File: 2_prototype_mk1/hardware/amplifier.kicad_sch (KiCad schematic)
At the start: 8 parts, among them U5 MAX98357A

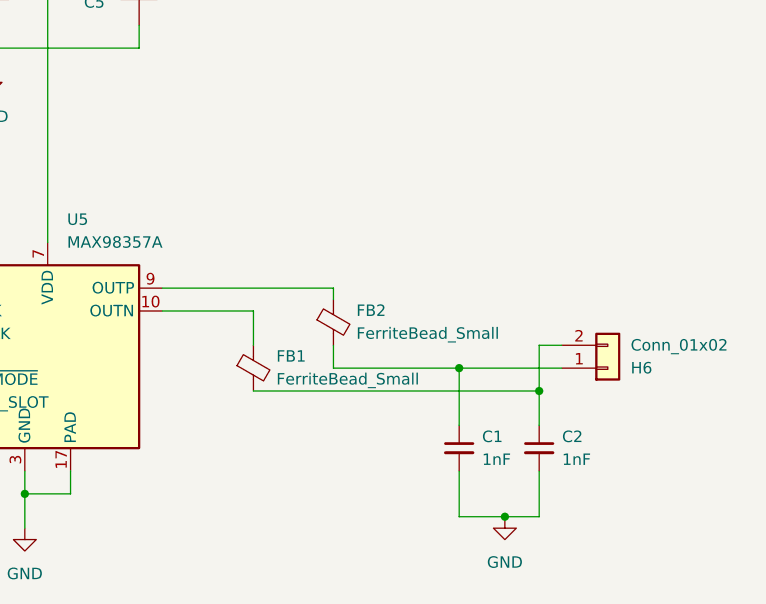
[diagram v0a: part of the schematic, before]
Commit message: Created basic PCB
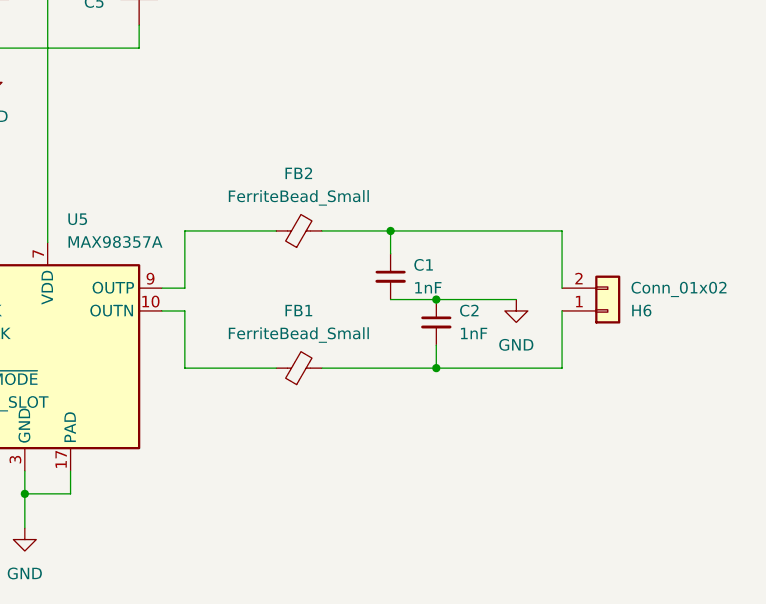
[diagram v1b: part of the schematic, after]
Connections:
- net GND: now also C2.1; no longer C2.2
- net at C1.1, FB2.2: now also H6.2 (Pin_2); no longer H6.1 (Pin_1)
- new net: C2.2, FB1.2, H6.1 (Pin_1)
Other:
- moved on the sheet: C1, C2, FB1, FB2, H6
